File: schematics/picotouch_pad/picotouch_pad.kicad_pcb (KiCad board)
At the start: 2 copper layers, 193.5 x 38 mm, 98 parts, among them J1 AudioJack4, SW1 SSSS811101, U1 Pico, U2 MCP73831-2-OT, X1 AFC20-S02ACA-00

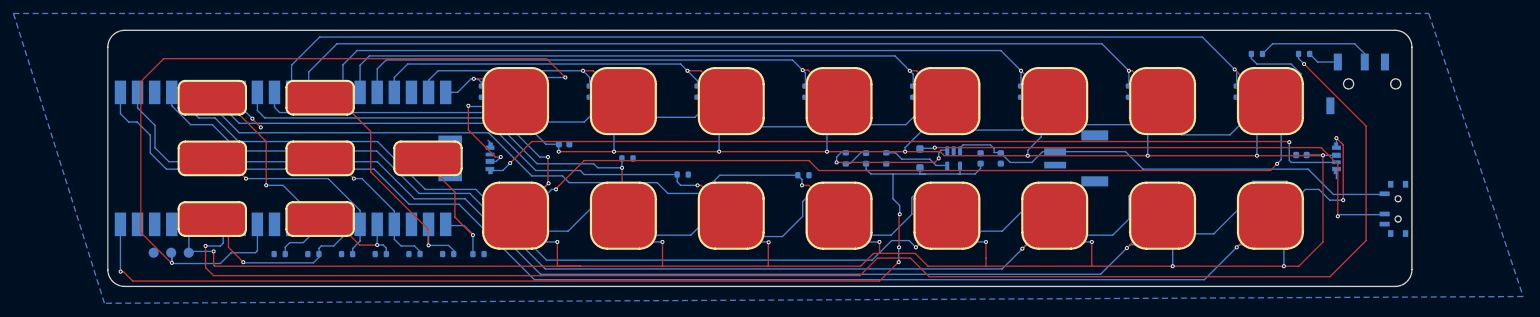
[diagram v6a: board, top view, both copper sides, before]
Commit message: new silkscreen and fixes
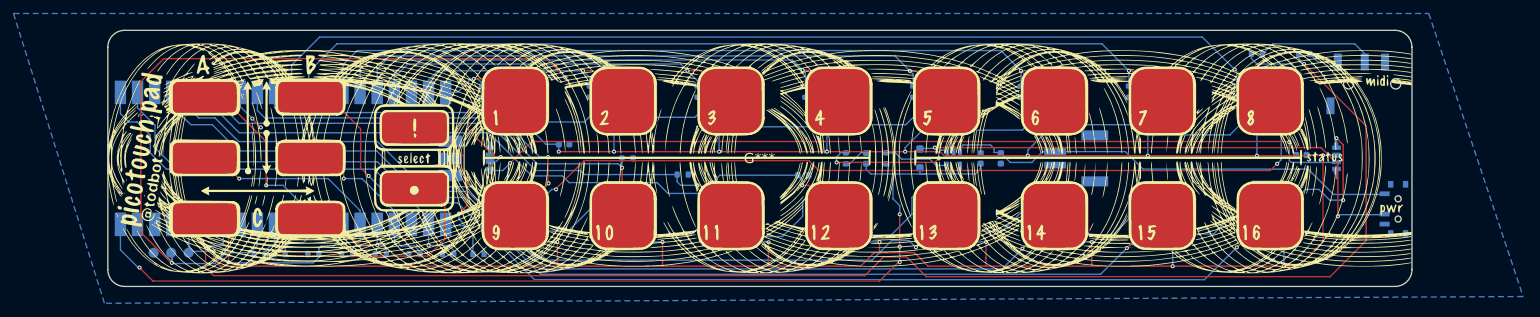
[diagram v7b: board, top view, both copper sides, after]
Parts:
- added G***: LOGO, LOGO, F.Cu at (110.8, 45.4)
- added PAD24: 1, todbot_stuff:Pad-CapTouch-10x5mm-roundrect, F.Cu at (59.6, 49.9)
- added R28: 1M, Resistor_SMD:R_0603_1608Metric, B.Cu at (36.6, 59.6)
- moved PAD17 4.92 mm to (59.6, 40.9)
- moved PAD18 1.50 mm to (44.1, 36.4)
- moved PAD19 1.50 mm to (44.1, 45.4)
- moved PAD20 1.50 mm to (44.1, 54.4)
- moved PAD21 1.00 mm to (28.6, 45.4)
- moved PAD22 1.00 mm to (28.6, 54.4)
- moved PAD23 1.00 mm to (28.6, 36.4)
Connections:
- U1 pad 31: unconnected-(U1-GPIO26_ADC0-Pad31) -> /TOUCH24
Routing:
- net /TOUCH24: track 0.00 -> 43.8 mm, vias 0 -> 1
- net /TOUCH17: track 22.8 -> 29.1 mm, vias 1 -> 2
- net /TOUCH22: track 29.1 -> 31.4 mm
- net +5V: track 160.9 -> 159.1 mm
- net /TOUCH18: track 38.6 -> 37.1 mm, vias 1 -> 2
- net /TOUCH23: track 34.1 -> 35.1 mm
- net /TOUCH19: track 21.4 -> 22.3 mm
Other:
- board text added: "${REFERENCE}"
- board text added: "VBUS"
